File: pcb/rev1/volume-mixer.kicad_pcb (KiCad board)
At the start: 2 copper layers, 34 parts, among them CON1 TC2030-IDC, Q1 2N7002, SW2 SW_Push, U1 STM32F302C8Tx, U3 XC6206PxxxMR, U4 XC6206PxxxMR, U5 PRTR5V0U2X, U6 TCA9548APWR, Y1 8MHz

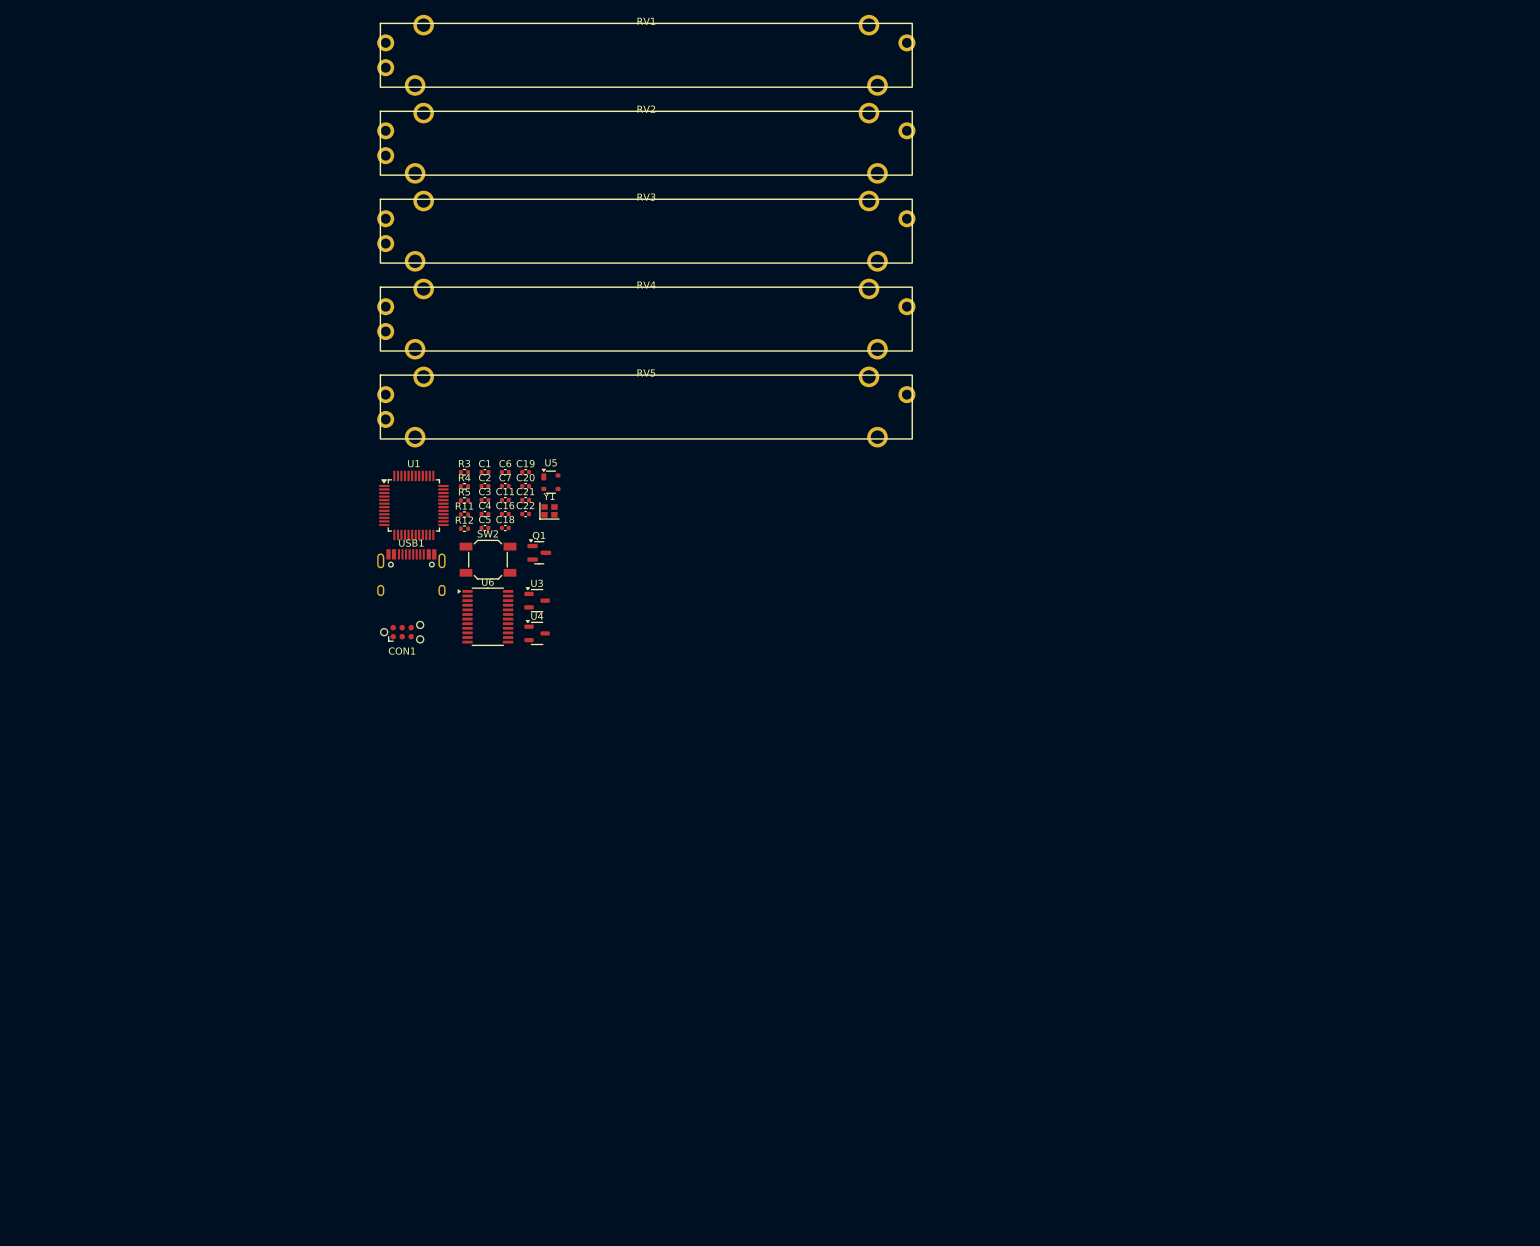
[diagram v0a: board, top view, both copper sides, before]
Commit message: avancer du layout
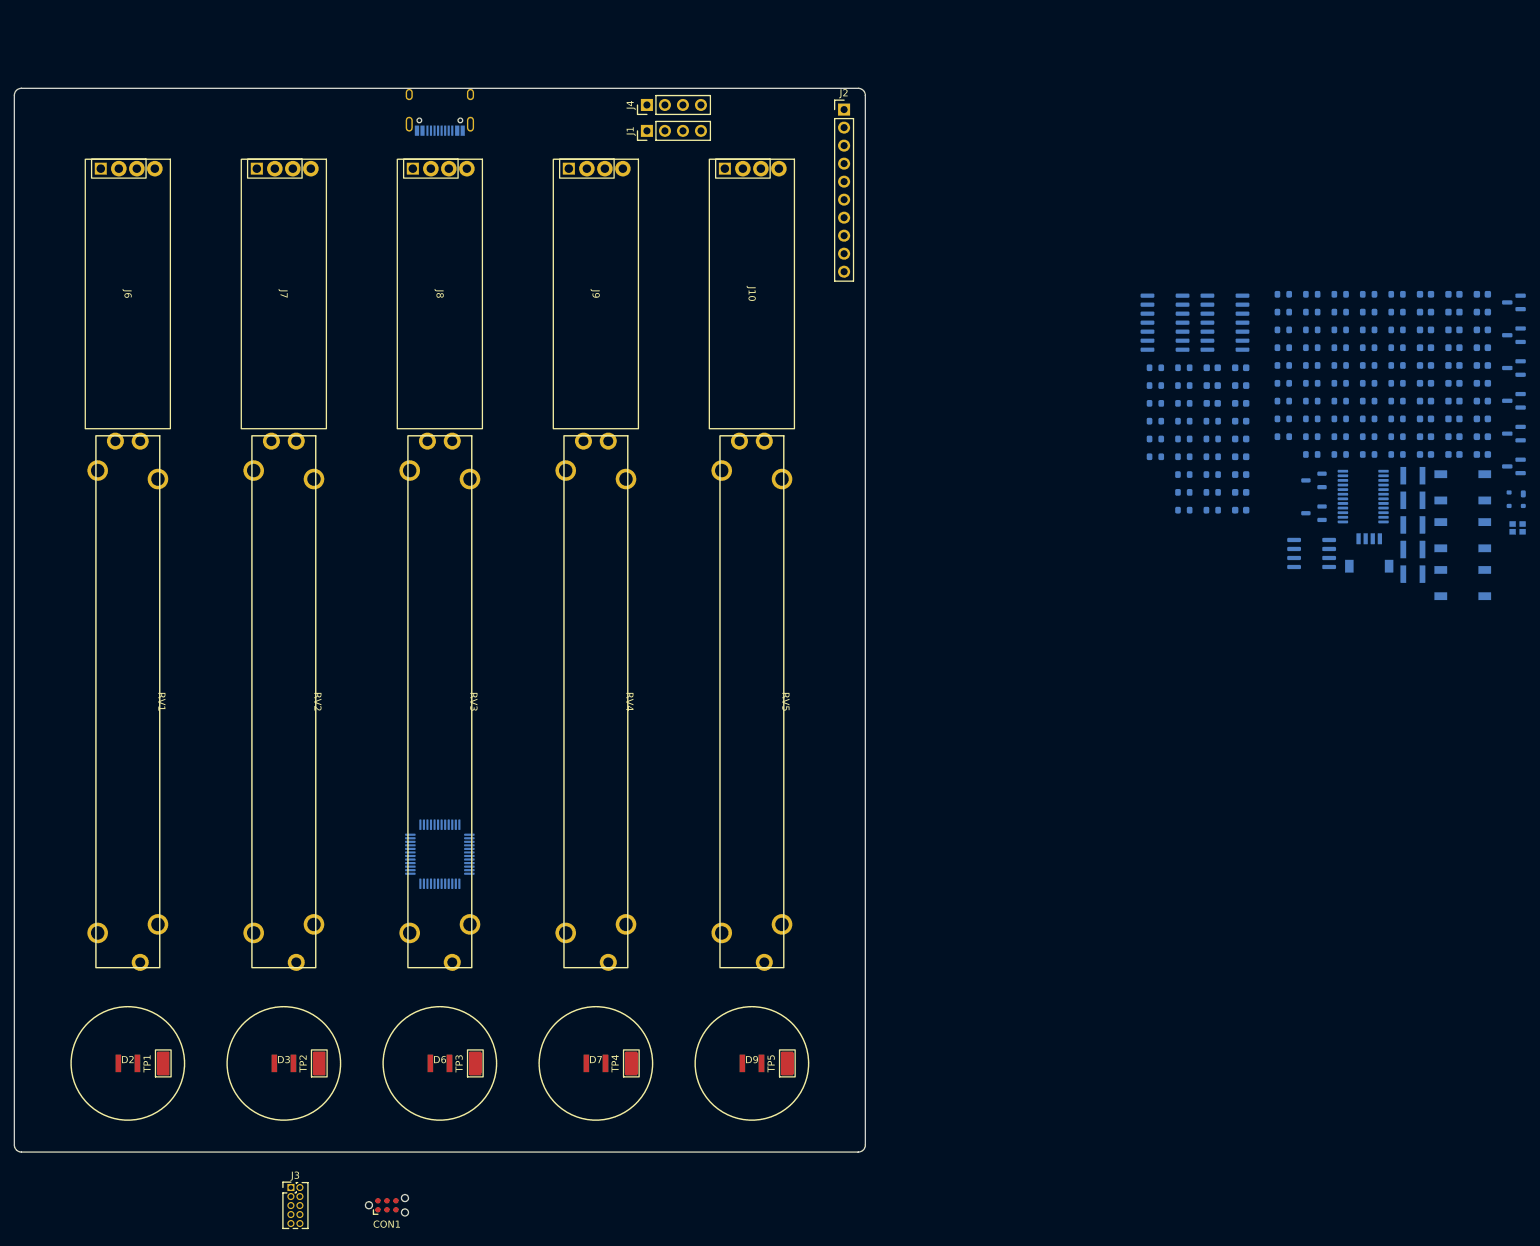
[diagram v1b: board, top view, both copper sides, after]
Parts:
- added C10: 47nF NP0, Capacitor_SMD:C_0603_1608Metric, B.Cu at (251.0, 85.1)
- added C12: 100nF, Capacitor_SMD:C_0603_1608Metric, B.Cu at (247.0, 65.1)
- added C13: 100nF, Capacitor_SMD:C_0603_1608Metric, B.Cu at (247.0, 67.6)
- added C14: 4,7uF, Capacitor_SMD:C_0603_1608Metric, B.Cu at (247.0, 70.1)
- added C15: 47nF NP0, Capacitor_SMD:C_0603_1608Metric, B.Cu at (247.0, 72.6)
- added C17: 2,2uF, Capacitor_SMD:C_0603_1608Metric, B.Cu at (247.0, 77.6)
- added C23: 100nF, Capacitor_SMD:C_0603_1608Metric, B.Cu at (243.0, 67.6)
- added C24: 100nF, Capacitor_SMD:C_0603_1608Metric, B.Cu at (243.0, 70.1)
- added C25: 100nF, Capacitor_SMD:C_0603_1608Metric, B.Cu at (243.0, 72.6)
- added C26: 100nF, Capacitor_SMD:C_0603_1608Metric, B.Cu at (243.0, 75.1)
- added C27: 100nF, Capacitor_SMD:C_0603_1608Metric, B.Cu at (243.0, 77.6)
- added C28: 100nF, Capacitor_SMD:C_0603_1608Metric, B.Cu at (243.0, 80.1)
- added C29: 100nF, Capacitor_SMD:C_0603_1608Metric, B.Cu at (243.0, 82.6)
- added C30: 100nF, Capacitor_SMD:C_0603_1608Metric, B.Cu at (243.0, 85.1)
- added C31: 100nF, Capacitor_SMD:C_0603_1608Metric, B.Cu at (216.9, 72.9)
- added C32: 680nF, Capacitor_SMD:C_0603_1608Metric, B.Cu at (216.9, 75.4)
- added C33: 100nF, Capacitor_SMD:C_0603_1608Metric, B.Cu at (216.9, 77.9)
- added C34: 100nF, Capacitor_SMD:C_0603_1608Metric, B.Cu at (216.9, 80.4)
- added C35: 100nF, Capacitor_SMD:C_0603_1608Metric, B.Cu at (216.9, 82.9)
- added C36: 680nF, Capacitor_SMD:C_0603_1608Metric, B.Cu at (216.9, 85.5)
- added C37: 100nF, Capacitor_SMD:C_0603_1608Metric, B.Cu at (216.9, 88.0)
- added C38: 680nF, Capacitor_SMD:C_0603_1608Metric, B.Cu at (216.9, 90.5)
- added C39: 100nF, Capacitor_SMD:C_0603_1608Metric, B.Cu at (216.9, 93.0)
- added C40: 680nF, Capacitor_SMD:C_0603_1608Metric, B.Cu at (212.9, 72.9)
- added C41: 100nF, Capacitor_SMD:C_0603_1608Metric, B.Cu at (212.9, 75.4)
- added C42: 680nF, Capacitor_SMD:C_0603_1608Metric, B.Cu at (212.9, 77.9)
- added C8: 47nF, Capacitor_SMD:C_0603_1608Metric, B.Cu at (251.0, 80.1)
- added C9: 100nF, Capacitor_SMD:C_0603_1608Metric, B.Cu at (251.0, 82.6)
- added D1: LED, A_Please:LED C516299, B.Cu at (241.2, 88.1)
- added D10: LED, A_Please:LED C516299, B.Cu at (241.2, 91.6)
- added D11: LED, A_Please:LED C516299, B.Cu at (241.2, 95.1)
- added D12: LED, A_Please:LED C516299, B.Cu at (241.2, 98.5)
- added D13: LED, A_Please:LED C516299, B.Cu at (241.2, 102.0)
- added D2: LED, A_Please:LED C516299, F.Cu at (60.0, 171.0)
- added D3: LED, A_Please:LED C516299, F.Cu at (82.0, 171.0)
- added D6: LED, A_Please:LED C516299, F.Cu at (104.0, 171.0)
- added D7: LED, A_Please:LED C516299, F.Cu at (126.0, 171.0)
- added D9: LED, A_Please:LED C516299, F.Cu at (148.0, 171.0)
- added J1: Conn_01x04_Pin, Connector_PinHeader_2.54mm:PinHeader_1x04_P2.54mm_Vertical, F.Cu at (133.2, 39.5)
- added J10: Conn_01x04_Pin, A_Please:Screen 0.91 I2C, F.Cu at (148.0, 44.8)
- added J2: Conn_01x10_Pin, Connector_PinHeader_2.54mm:PinHeader_1x10_P2.54mm_Vertical, F.Cu at (161.0, 36.5)
- added J3: Conn_01x10_Pin, Connector_PinHeader_1.27mm:PinHeader_2x05_P1.27mm_Vertical, F.Cu at (83.0, 188.5)
- added J4: Conn_01x04_Pin, Connector_PinHeader_2.54mm:PinHeader_1x04_P2.54mm_Vertical, F.Cu at (133.2, 35.9)
- added J5: JST, A_random_part:JST-SR-4, B.Cu at (235.1, 101.8)
- added J6: Conn_01x04_Pin, A_Please:Screen 0.91 I2C, F.Cu at (60.0, 44.8)
- added J7: Conn_01x04_Pin, A_Please:Screen 0.91 I2C, F.Cu at (82.0, 44.8)
- added J8: Conn_01x04_Pin, A_Please:Screen 0.91 I2C, F.Cu at (104.0, 44.8)
- added J9: Conn_01x04_Pin, A_Please:Screen 0.91 I2C, F.Cu at (126.0, 44.8)
- added Q10: NMOS, Package_TO_SOT_SMD:SOT-23, B.Cu at (255.5, 86.8)
- added Q3: NMOS, Package_TO_SOT_SMD:SOT-23, B.Cu at (255.5, 68.3)
- added Q7: NMOS, Package_TO_SOT_SMD:SOT-23, B.Cu at (255.5, 72.9)
- added Q8: NMOS, Package_TO_SOT_SMD:SOT-23, B.Cu at (255.5, 77.6)
- added Q9: NMOS, Package_TO_SOT_SMD:SOT-23, B.Cu at (255.5, 82.2)
- added R1: 10k, Resistor_SMD:R_0603_1608Metric, B.Cu at (239.0, 62.5)
- added R10: 10k, Resistor_SMD:R_0603_1608Metric, B.Cu at (239.0, 85.1)
- added R13: 1k2, Resistor_SMD:R_0603_1608Metric, B.Cu at (235.0, 67.6)
- added R15: 100, Resistor_SMD:R_0603_1608Metric, B.Cu at (235.0, 70.1)
- added R16: 1k2, Resistor_SMD:R_0603_1608Metric, B.Cu at (235.0, 72.6)
- added R17: 4,7K, Resistor_SMD:R_0603_1608Metric, B.Cu at (235.0, 75.1)
- added R18: 4,7K, Resistor_SMD:R_0603_1608Metric, B.Cu at (235.0, 77.6)
- added R19: 1k2, Resistor_SMD:R_0603_1608Metric, B.Cu at (235.0, 80.1)
- added R2: 10k, Resistor_SMD:R_0603_1608Metric, B.Cu at (239.0, 65.1)
- added R22: 1k2, Resistor_SMD:R_0603_1608Metric, B.Cu at (235.0, 82.6)
- added R24: 4,7K, Resistor_SMD:R_0603_1608Metric, B.Cu at (235.0, 85.1)
- added R25: 4,7K, Resistor_SMD:R_0603_1608Metric, B.Cu at (231.0, 62.5)
- added R26: 4,7K, Resistor_SMD:R_0603_1608Metric, B.Cu at (231.0, 65.1)
- added R27: 4,7K, Resistor_SMD:R_0603_1608Metric, B.Cu at (231.0, 67.6)
- added R28: 4,7K, Resistor_SMD:R_0603_1608Metric, B.Cu at (231.0, 70.1)
- added R29: 4,7K, Resistor_SMD:R_0603_1608Metric, B.Cu at (231.0, 72.6)
- added R30: 4,7K, Resistor_SMD:R_0603_1608Metric, B.Cu at (231.0, 75.1)
- added R31: 4,7K, Resistor_SMD:R_0603_1608Metric, B.Cu at (231.0, 77.6)
- added R32: 4,7K, Resistor_SMD:R_0603_1608Metric, B.Cu at (231.0, 80.1)
- added R33: 4,7K, Resistor_SMD:R_0603_1608Metric, B.Cu at (231.0, 82.6)
- added R34: 4,7K, Resistor_SMD:R_0603_1608Metric, B.Cu at (231.0, 85.1)
- added R35: 4,7K, Resistor_SMD:R_0603_1608Metric, B.Cu at (226.9, 62.5)
- added R36: 4,7K, Resistor_SMD:R_0603_1608Metric, B.Cu at (226.9, 65.1)
- added R37: 4,7K, Resistor_SMD:R_0603_1608Metric, B.Cu at (226.9, 67.6)
- added R38: 4,7K, Resistor_SMD:R_0603_1608Metric, B.Cu at (226.9, 70.1)
- added R39: 4,7K, Resistor_SMD:R_0603_1608Metric, B.Cu at (226.9, 72.6)
- added R40: 2K, Resistor_SMD:R_0603_1608Metric, B.Cu at (212.9, 80.4)
- added R41: 20K, Resistor_SMD:R_0603_1608Metric, B.Cu at (212.9, 82.9)
- added R42: 2K, Resistor_SMD:R_0603_1608Metric, B.Cu at (212.9, 85.5)
- added R43: 2K, Resistor_SMD:R_0603_1608Metric, B.Cu at (212.9, 88.0)
- added R44: 20K, Resistor_SMD:R_0603_1608Metric, B.Cu at (212.9, 90.5)
- added R45: 2K, Resistor_SMD:R_0603_1608Metric, B.Cu at (212.9, 93.0)
- added R46: 10k, Resistor_SMD:R_0603_1608Metric, B.Cu at (208.9, 72.9)
- added R47: 10k, Resistor_SMD:R_0603_1608Metric, B.Cu at (208.9, 75.4)
- added R48: 2K, Resistor_SMD:R_0603_1608Metric, B.Cu at (208.9, 77.9)
- added R49: 10k, Resistor_SMD:R_0603_1608Metric, B.Cu at (208.9, 80.4)
- added R50: 20K, Resistor_SMD:R_0603_1608Metric, B.Cu at (208.9, 82.9)
- added R51: 10k, Resistor_SMD:R_0603_1608Metric, B.Cu at (208.9, 85.5)
- added R52: 2K, Resistor_SMD:R_0603_1608Metric, B.Cu at (208.9, 88.0)
- added R53: 10k, Resistor_SMD:R_0603_1608Metric, B.Cu at (208.9, 90.5)
- added R54: 10k, Resistor_SMD:R_0603_1608Metric, B.Cu at (208.9, 93.0)
- added R55: 2K, Resistor_SMD:R_0603_1608Metric, B.Cu at (204.9, 72.9)
- added R56: 20K, Resistor_SMD:R_0603_1608Metric, B.Cu at (204.9, 75.4)
- added R57: 2K, Resistor_SMD:R_0603_1608Metric, B.Cu at (204.9, 77.9)
- added R58: 2K, Resistor_SMD:R_0603_1608Metric, B.Cu at (204.9, 80.4)
- added R59: 20K, Resistor_SMD:R_0603_1608Metric, B.Cu at (204.9, 82.9)
- added R6: 10k, Resistor_SMD:R_0603_1608Metric, B.Cu at (239.0, 75.1)
- added R60: 2K, Resistor_SMD:R_0603_1608Metric, B.Cu at (204.9, 85.5)
- added R61: 100, Resistor_SMD:R_0603_1608Metric, B.Cu at (226.9, 75.1)
- added R62: 10K, Resistor_SMD:R_0603_1608Metric, B.Cu at (226.9, 77.6)
- added R63: 10K, Resistor_SMD:R_0603_1608Metric, B.Cu at (226.9, 80.1)
- added R64: 100, Resistor_SMD:R_0603_1608Metric, B.Cu at (226.9, 82.6)
- added R65: 100, Resistor_SMD:R_0603_1608Metric, B.Cu at (226.9, 85.1)
- added R66: 10K, Resistor_SMD:R_0603_1608Metric, B.Cu at (222.9, 62.5)
- added R67: 100, Resistor_SMD:R_0603_1608Metric, B.Cu at (222.9, 65.1)
- added R68: 100, Resistor_SMD:R_0603_1608Metric, B.Cu at (222.9, 67.6)
- added R69: 10K, Resistor_SMD:R_0603_1608Metric, B.Cu at (222.9, 70.1)
- added R7: 10k, Resistor_SMD:R_0603_1608Metric, B.Cu at (239.0, 77.6)
- added R70: 100, Resistor_SMD:R_0603_1608Metric, B.Cu at (222.9, 72.6)
- added R71: 100, Resistor_SMD:R_0603_1608Metric, B.Cu at (222.9, 75.1)
- added R72: 10K, Resistor_SMD:R_0603_1608Metric, B.Cu at (222.9, 77.6)
- added R73: 100, Resistor_SMD:R_0603_1608Metric, B.Cu at (222.9, 80.1)
- added R74: 100, Resistor_SMD:R_0603_1608Metric, B.Cu at (222.9, 82.6)
- added R8: 10k, Resistor_SMD:R_0603_1608Metric, B.Cu at (239.0, 80.1)
- added R9: 10k, Resistor_SMD:R_0603_1608Metric, B.Cu at (239.0, 82.6)
- added SW1: SW_Push, Button_Switch_SMD:SW_SPST_SKQG_WithStem, B.Cu at (248.2, 89.8)
- added SW3: SW_Push, Button_Switch_SMD:SW_SPST_SKQG_WithStem, B.Cu at (248.2, 103.3)
- added TP1: TestPoint_Flag, TestPoint:TestPoint_Keystone_5015_Micro_Mini, F.Cu at (65.0, 171.0)
- added TP2: TestPoint_Flag, TestPoint:TestPoint_Keystone_5015_Micro_Mini, F.Cu at (87.0, 171.0)
- added TP3: TestPoint_Flag, TestPoint:TestPoint_Keystone_5015_Micro_Mini, F.Cu at (109.0, 171.0)
- added TP4: TestPoint_Flag, TestPoint:TestPoint_Keystone_5015_Micro_Mini, F.Cu at (131.0, 171.0)
- added TP5: TestPoint_Flag, TestPoint:TestPoint_Keystone_5015_Micro_Mini, F.Cu at (153.0, 171.0)
- added U2: 24LC64, Package_SO:SOIC-8_3.9x4.9mm_P1.27mm, B.Cu at (226.9, 99.1)
- added U7: TL084, Package_SO:SOIC-14_3.9x8.7mm_P1.27mm, B.Cu at (214.7, 66.5)
- added U8: TL084, Package_SO:SOIC-14_3.9x8.7mm_P1.27mm, B.Cu at (206.3, 66.5)
- C1, C19, C2, C20, C3, C4, C5, C6, C7: footprint Capacitor_SMD:C_0402_1005Metric -> Capacitor_SMD:C_0603_1608Metric; moved to B.Cu
- C11: value 47nF -> 100nF; footprint Capacitor_SMD:C_0402_1005Metric -> Capacitor_SMD:C_0603_1608Metric; moved to B.Cu
- C16: value 4,7uF -> 470nF; footprint Capacitor_SMD:C_0402_1005Metric -> Capacitor_SMD:C_0603_1608Metric; moved to B.Cu
- C18: value 470nF -> 2,2uF; footprint Capacitor_SMD:C_0402_1005Metric -> Capacitor_SMD:C_0603_1608Metric; moved to B.Cu
- C21, C22: value 2,2uF -> 100nF; footprint Capacitor_SMD:C_0402_1005Metric -> Capacitor_SMD:C_0603_1608Metric; moved to B.Cu
- Q1: value 2N7002 -> NMOS; moved to B.Cu
- R11, R12, R3, R4, R5: footprint Resistor_SMD:R_0402_1005Metric -> Resistor_SMD:R_0603_1608Metric; moved to B.Cu
- RV1, RV2, RV3, RV4, RV5: value R_Potentiometer_US -> PTA6043-2015CPB103
- SW2, U1, U3, U4, U5, U6, USB1, Y1: moved to B.Cu
- moved C1 142.9 mm to (251.0, 62.5), turned to 180 degrees
- moved C2 142.8 mm to (251.0, 65.1), turned to 180 degrees
- moved C3 142.7 mm to (251.0, 67.6), turned to 180 degrees
- moved C4 142.6 mm to (251.0, 70.1), turned to 180 degrees
- moved C5 142.5 mm to (251.0, 72.6), turned to 180 degrees
- moved Q1 141.9 mm to (255.5, 63.7), turned to 180 degrees
- moved C6 138.3 mm to (251.0, 75.1), turned to 180 degrees
- moved C7 138.3 mm to (251.0, 77.6), turned to 180 degrees
- moved SW2 137.5 mm to (248.2, 96.5), turned to 180 degrees
- moved C11 136.9 mm to (247.0, 62.5), turned to 180 degrees
- moved Y1 136.5 mm to (256.0, 95.5), turned to 180 degrees
- moved U5 136.1 mm to (255.8, 91.4), turned to 180 degrees
- moved C16 135.0 mm to (247.0, 75.1), turned to 180 degrees
- moved C18 134.7 mm to (247.0, 80.1), turned to 180 degrees
- moved R3 133.0 mm to (239.0, 67.6), turned to 180 degrees
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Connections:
- net /D+ renamed D+
- net /D- renamed D-
- C11 pad 1: GND -> +3V3
- C11 pad 2: +3V3 -> GND
- C16 pad 1: /BOOT -> /RESET
- C16 pad 2: Net-(Q1-G) -> GND
- C18 pad 1: /RESET -> +3V3
- C20 pad 1: +3V3 -> Vana
- C21 pad 1: VBUS -> +3V3
- C22 pad 1: Vana -> +3V3
- Q1 pad 1: Net-(Q1-G) -> /RESET
- Q1 pad 2: GND -> Net-(Q1-G)
- Q1 pad 3: /RESET -> GND
- RV1 pad M: (no net) -> GND
- RV2 pad M: (no net) -> GND
- RV3 pad M: (no net) -> GND
- RV4 pad M: (no net) -> GND
- RV5 pad M: (no net) -> GND
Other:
- board outline added: 120 x 150 mm

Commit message: blabla
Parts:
- moved Q3 224.3 mm to (59.1, 176.8)
- moved Q7 203.1 mm to (81.1, 177.1)
- moved U5 198.4 mm to (70.2, 21.3)
- moved Q8 181.0 mm to (103.8, 176.3)
- moved R38 170.9 mm to (374.9, 155.5)
- moved R39 170.9 mm to (374.9, 158.1)
- moved R11 170.8 mm to (67.9, 26.9)
- moved R36 169.5 mm to (370.5, 155.2)
- moved R37 169.5 mm to (370.5, 157.7)
- moved R35 168.1 mm to (365.4, 157.9)
- moved R12 167.3 mm to (72.0, 27.2)
- moved Q9 160.6 mm to (125.5, 176.5)
- moved R6 159.9 mm to (93.8, 142.0), turned to 0 degrees
- moved R7 159.7 mm to (93.8, 144.0), turned to 0 degrees
- moved U2 157.9 mm to (379.2, 141.0)
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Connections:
- U1 pad 25: SLIDER 3 mute  -> SLIDER 4 mute 
- U1 pad 26: SLIDER 4 mute  -> SLIDER 3 mute 
- U1 pad 39: SLIDER 0 mute  -> SLIDER 1 mute 
- U1 pad 40: SLIDER 1 mute  -> SLIDER 0 mute 
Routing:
- net Net-(R10-Pad1): track 0.00 -> 55.8 mm, vias 0 -> 1
- net Net-(R6-Pad1): track 0.00 -> 45.2 mm, vias 0 -> 3
- net Net-(R9-Pad1): track 0.00 -> 34.7 mm, vias 0 -> 1
- net Net-(R8-Pad1): track 0.00 -> 29.1 mm, vias 0 -> 3
- net Net-(R7-Pad1): track 0.00 -> 27.2 mm, vias 0 -> 3
- net SLIDER 3 mute : track 0.00 -> 7.26 mm
- net SLIDER 4 mute : track 0.00 -> 6.97 mm
- net SLIDER 0 mute : track 0.00 -> 5.55 mm
- net SLIDER 1 mute : track 0.00 -> 5.54 mm
- net SLIDER 2 mute : track 0.00 -> 4.18 mm
- added copper zone on B.Cu, net GND
- added copper zone on F.Cu, net GND
- added copper zone on In1.Cu, net GND
- added copper zone on In2.Cu, net GND
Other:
- copper layers 2 -> 4

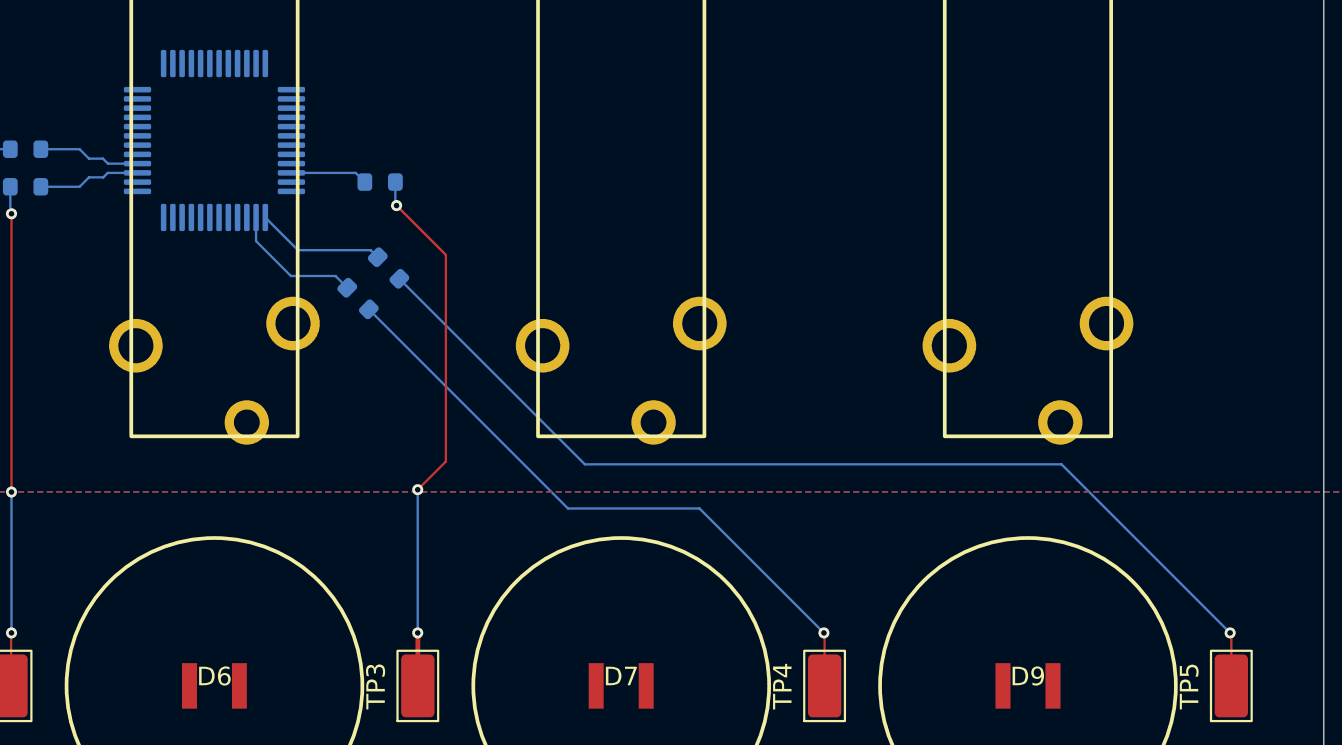
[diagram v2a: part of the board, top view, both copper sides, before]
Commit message: Capacitive sensor layout
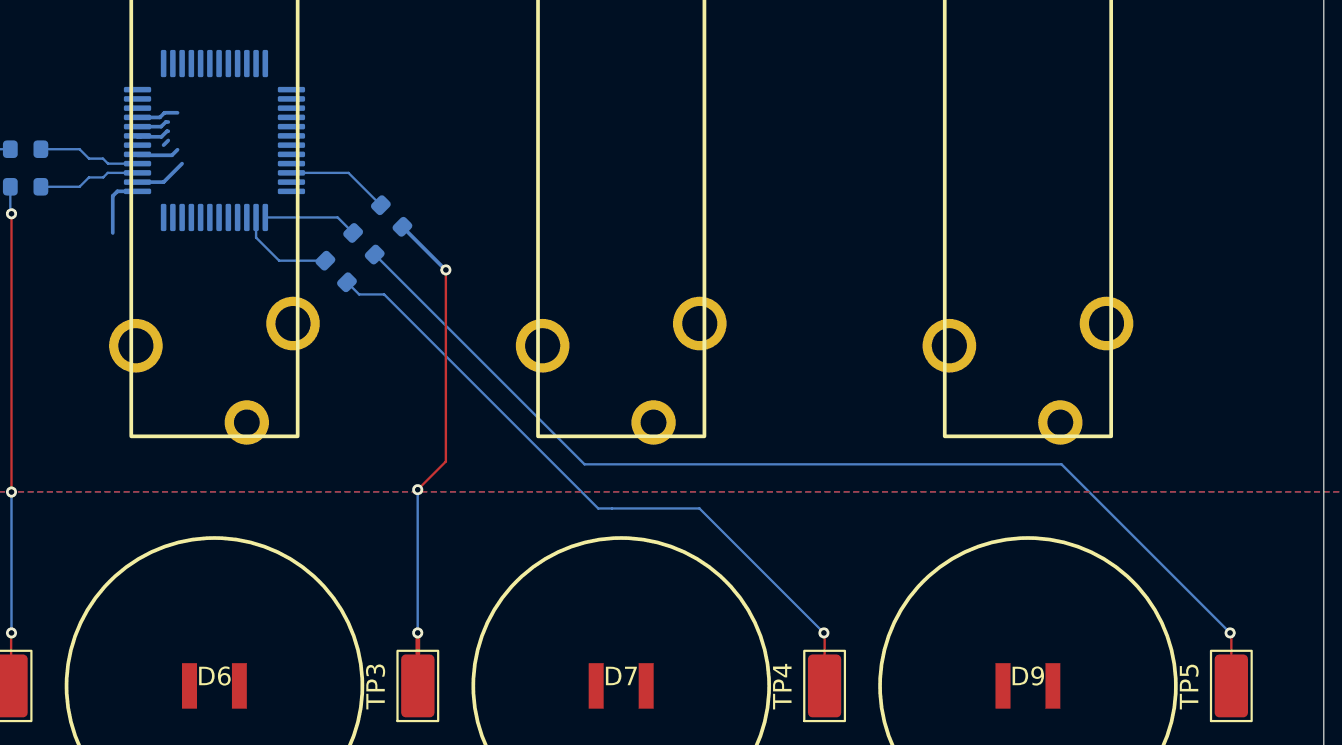
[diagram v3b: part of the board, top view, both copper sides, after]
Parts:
- moved R8 1.94 mm to (113.6, 145.6), turned to 135 degrees
- moved R9 1.88 mm to (110.6, 148.6)
- moved R10 1.87 mm to (112.1, 147.1)
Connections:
- net Net-(R10-Pad1) renamed /SliderSense4
- net Net-(R6-Pad1) renamed /SliderSense0
- net Net-(R7-Pad1) renamed /SliderSense1
- net Net-(R8-Pad1) renamed /SliderSense2
- net Net-(R9-Pad1) renamed /SliderSense3
- net Net-(U1-PB14) renamed /CapSense1
- net Net-(U1-PB6) renamed /CapSense0
- net SLIDER 0 mute  renamed SLIDER_0_mute 
- net SLIDER 1 mute  renamed SLIDER_1_mute 
- net SLIDER 2 mute  renamed SLIDER_2_mute 
- net SLIDER 3 mute  renamed SLIDER_3_mute 
- net SLIDER 4 mute  renamed SLIDER_4_mute 
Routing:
- net /SWCLK: track 0.00 -> 3.44 mm
- net Mute0Led: track 0.00 -> 2.83 mm
- net /SliderSense2: track 29.1 -> 26.5 mm
- net /SliderSense4: track 55.8 -> 58.2 mm
- net DBG IO1: track 0.00 -> 2.34 mm
- net DBG RX: track 0.00 -> 2.27 mm
- net SLIDER_3_mute : track 7.26 -> 5.36 mm
- net SLIDER_4_mute : track 6.97 -> 5.10 mm
- net DBG IO0: track 0.00 -> 1.84 mm
- net /SliderSense3: track 34.7 -> 36.5 mm
- net /BOOT: track 0.00 -> 1.77 mm
- net SLIDER_2_mute : track 4.18 -> 5.56 mm
